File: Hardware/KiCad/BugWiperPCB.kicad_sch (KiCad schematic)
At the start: 11 parts, among them J2 TBLH10-350-06BK, J3 Phoenix_1776508

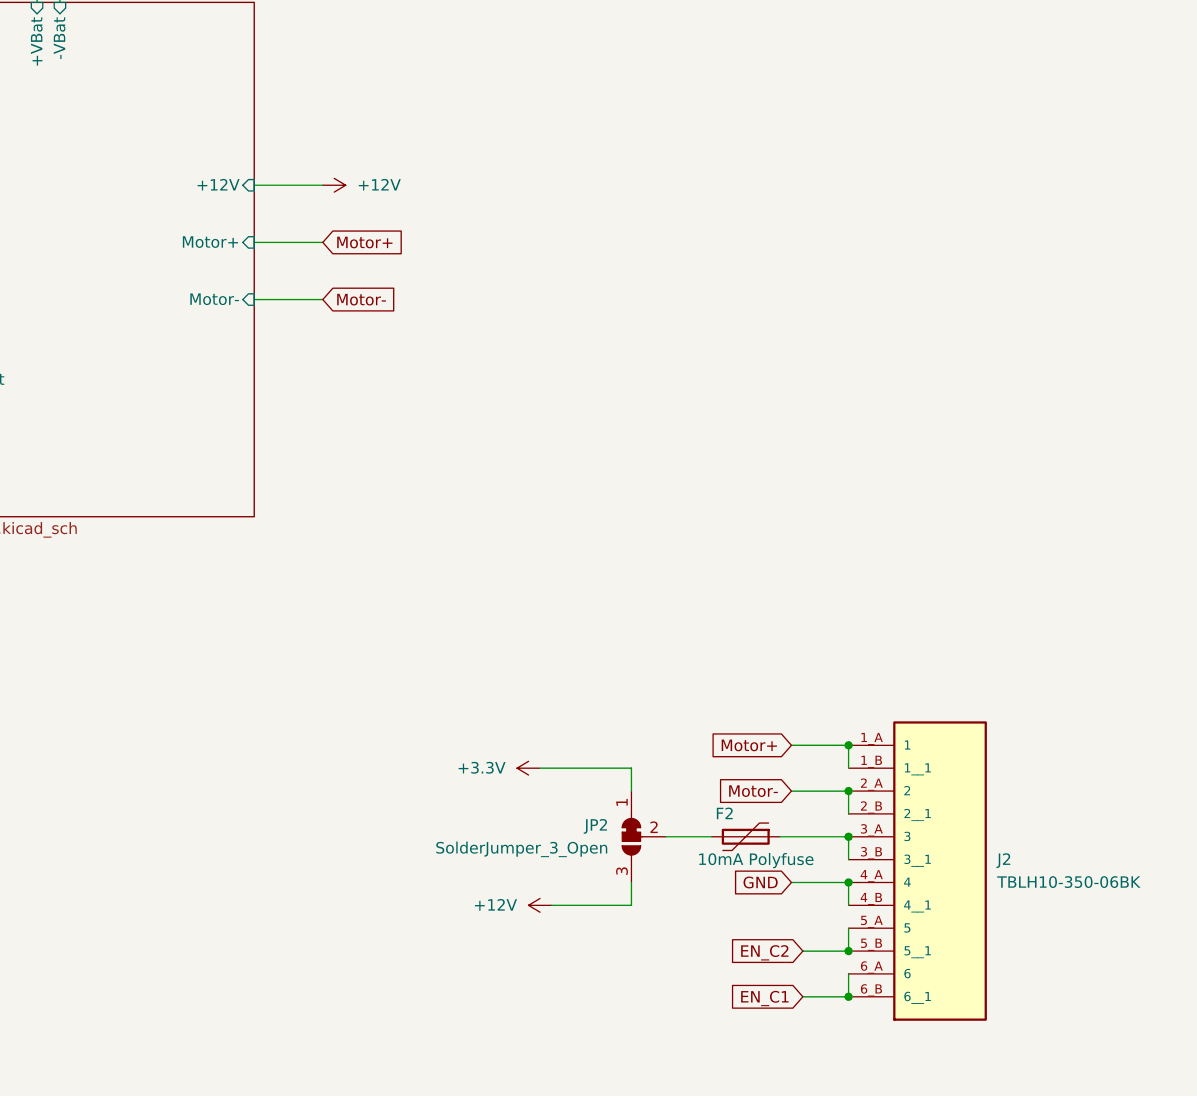
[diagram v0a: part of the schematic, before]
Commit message: update PCB, routing and Connector
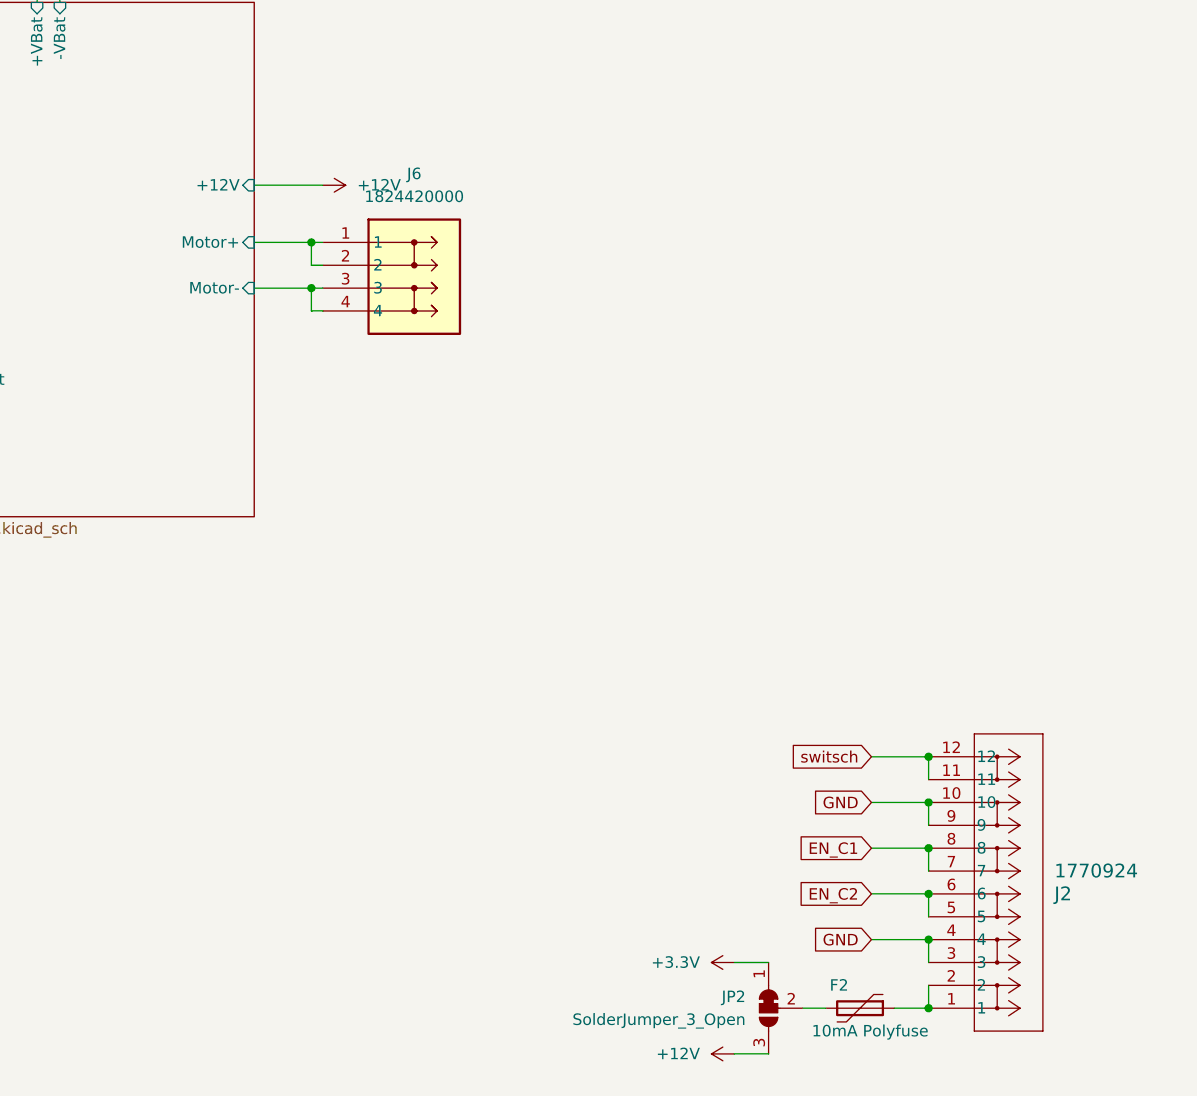
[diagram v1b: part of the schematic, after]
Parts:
- removed J2: TBLH10-350-06BK, TBLH10_350_06BK-2:CUI_TBLH10-350-06BK, symbol TBLH10-350-06BK:TBLH10-350-06BK
- added J2: 1770924, CONN_1814537, symbol BugWiper_Lib:1770924
- added J6: 1824420000, SHDR4W80P700X350_2X2_770X1400X850P, symbol BugWiper_Lib:1824420000
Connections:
- net EN_C1: now also J2.7, J2.8
- net EN_C2: now also J2.5, J2.6
- net GND: now also J2.10, J2.3, J2.4, J2.9
- net at F2.1: now also J2.1, J2.2
- new net Power/Motor+: J6.1, J6.2
- new net Power/Motor-: J6.3, J6.4
- new net switsch: J2.11, J2.12
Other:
- moved on the sheet: F2, JP2

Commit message: update PCB
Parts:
- renumbered H5 to H2, H2 to H5
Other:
- moved on the sheet: C27, H2, H5, R27
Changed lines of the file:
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@@
 (kicad_sch (version 20230121) (generator eeschema)
   (paper "A4")
-  (junction (at 81.28 158.75) (diameter 0) (color 0 0 0 0)
-  )
-  (junction (at 81.28 148.59) (diameter 0) (color 0 0 0 0)
+  (junction (at 114.3 176.53) (diameter 0) (color 0 0 0 0)
+  )
+  (junction (at 114.3 166.37) (diameter 0) (color 0 0 0 0)
   )
   (junction (at 255.27 151.13) (diameter 0) (color 0 0 0 0)
@@
     (stroke (width 0) (type default))
   )
-  (wire (pts (xy 77.47 158.75) (xy 77.47 157.48))
+  (wire (pts (xy 110.49 176.53) (xy 110.49 175.26))
     (stroke (width 0) (type default))
   )
@@
     (stroke (width 0) (type default))
   )
-  (wire (pts (xy 81.28 158.75) (xy 81.28 160.02))
+  (wire (pts (xy 114.3 176.53) (xy 114.3 177.8))
     (stroke (width 0) (type default))
   )
@@
     (stroke (width 0) (type default))
   )
-  (wire (pts (xy 77.47 148.59) (xy 81.28 148.59))
+  (wire (pts (xy 110.49 166.37) (xy 114.3 166.37))
     (stroke (width 0) (type default))
   )
@@
     (stroke (width 0) (type default))
   )
-  (wire (pts (xy 81.28 158.75) (xy 81.28 157.48))
-    (stroke (width 0) (type default))
-  )
-  (wire (pts (xy 77.47 158.75) (xy 81.28 158.75))
+  (wire (pts (xy 114.3 176.53) (xy 114.3 175.26))
+    (stroke (width 0) (type default))
+  )
+  (wire (pts (xy 110.49 176.53) (xy 114.3 176.53))
     (stroke (width 0) (type default))
   )
@@
     (stroke (width 0) (type default))
   )
-  (wire (pts (xy 81.28 148.59) (xy 81.28 149.86))
-    (stroke (width 0) (type default))
-  )
-  (wire (pts (xy 77.47 148.59) (xy 77.47 149.86))
+  (wire (pts (xy 114.3 166.37) (xy 114.3 167.64))
+    (stroke (width 0) (type default))
+  )
+  (wire (pts (xy 110.49 166.37) (xy 110.49 167.64))
     (stroke (width 0) (type default))
   )
@@
     )
   )
-  (symbol (lib_id "Device:C") (at 77.47 153.67 0) (mirror y) (unit 1)
+  (symbol (lib_id "Device:C") (at 110.49 171.45 0) (mirror y) (unit 1)
     (in_bom yes) (on_board yes) (dnp no)
-    (property "Reference" "C27" (at 73.66 152.4 0)
-      (effects (font (size 1.27 1.27)) (justify left))
-    )
-    (property "Value" "100nF" (at 73.66 154.94 0)
-      (effects (font (size 1.27 1.27)) (justify left))
-    )
-    (property "Footprint" "Capacitor_SMD:C_0603_1608Metric" (at 76.5048 157.48 0)
-      (effects (font (size 1.27 1.27)) hide)
-    )
-    (property "Datasheet" "~" (at 77.47 153.67 0)
+    (property "Reference" "C27" (at 106.68 170.18 0)
+      (effects (font (size 1.27 1.27)) (justify left))
+    )
+    (property "Value" "100nF" (at 106.68 172.72 0)
+      (effects (font (size 1.27 1.27)) (justify left))
+    )
+    (property "Footprint" "Capacitor_SMD:C_0603_1608Metric" (at 109.5248 175.26 0)
+      (effects (font (size 1.27 1.27)) hide)
+    )
+    (property "Datasheet" "~" (at 110.49 171.45 0)
       (effects (font (size 1.27 1.27)) hide)
     )
@@
     )
   )
-  (symbol (lib_id "Mechanical:MountingHole_Pad") (at 81.28 146.05 0) (unit 1)
-    (in_bom yes) (on_board yes) (dnp no) (fields_autoplaced)
-    (property "Reference" "H2" (at 83.82 143.51 0)
-      (effects (font (size 1.27 1.27)) (justify left))
-    )
-    (property "Value" "MountingHole_Pad" (at 83.82 146.05 0)
-      (effects (font (size 1.27 1.27)) (justify left))
-    )
-    (property "Footprint" "MountingHole:MountingHole_3.2mm_M3_DIN965_Pad_TopBottom" (at 81.28 146.05 0)
-      (effects (font (size 1.27 1.27)) hide)
-    )
-    (property "Datasheet" "~" (at 81.28 146.05 0)
-      (effects (font (size 1.27 1.27)) hide)
-    )
-    (pin "1")
+  (symbol (lib_id "Mechanical:MountingHole_Pad") (at 114.3 163.83 0) (unit 1)
+    (in_bom yes) (on_board yes) (dnp no) (fields_autoplaced)
+    (property "Reference" "H5" (at 116.84 161.29 0)
+      (effects (font (size 1.27 1.27)) (justify left))
+    )
+    (property "Value" "MountingHole_Pad" (at 116.84 163.83 0)
+      (effects (font (size 1.27 1.27)) (justify left))
+    )
+    (property "Footprint" "MountingHole:MountingHole_3.2mm_M3_DIN965_Pad_TopBottom" (at 114.3 163.83 0)
+      (effects (font (size 1.27 1.27)) hide)
+    )
+    (property "Datasheet" "~" (at 114.3 163.83 0)
+      (effects (font (size 1.27 1.27)) hide)
+    )
+    (pin "1")
+    (instances
+      (project "BugWiperPCB"
+        (path "/d31a15bd-db02-4d4c-9593-17c596d3182c"
+          (reference "H5") (unit 1)
+        )
+      )
+    )
+  )
+  (symbol (lib_id "power:GND") (at 114.3 177.8 0) (unit 1)
+    (in_bom yes) (on_board yes) (dnp no) (fields_autoplaced)
+    (property "Reference" "#PWR034" (at 114.3 184.15 0)
+      (effects (font (size 1.27 1.27)) hide)
+    )
+    (property "Value" "GND" (at 114.3 182.88 0)
+      (effects (font (size 1.27 1.27)))
+    )
+    (property "Footprint" "" (at 114.3 177.8 0)
+      (effects (font (size 1.27 1.27)) hide)
+    )
+    (property "Datasheet" "" (at 114.3 177.8 0)
+      (effects (font (size 1.27 1.27)) hide)
+    )
+    (pin "1")
+    (instances
+      (project "BugWiperPCB"
+        (path "/d31a15bd-db02-4d4c-9593-17c596d3182c"
+          (reference "#PWR034") (unit 1)
+        )
+      )
+    )
+  )
+  (symbol (lib_id "Mechanical:MountingHole") (at 82.55 144.78 0) (unit 1)
+    (in_bom yes) (on_board yes) (dnp no) (fields_autoplaced)
+    (property "Reference" "H2" (at 85.09 143.51 0)
+      (effects (font (size 1.27 1.27)) (justify left))
+    )
+    (property "Value" "MountingHole" (at 85.09 146.05 0)
+      (effects (font (size 1.27 1.27)) (justify left))
+    )
+    (property "Footprint" "MountingHole:MountingHole_3.2mm_M3_DIN965" (at 82.55 144.78 0)
+      (effects (font (size 1.27 1.27)) hide)
+    )
+    (property "Datasheet" "~" (at 82.55 144.78 0)
+      (effects (font (size 1.27 1.27)) hide)
+    )
     (instances
       (project "BugWiperPCB"
@@
     )
   )
-  (symbol (lib_id "power:GND") (at 81.28 160.02 0) (unit 1)
-    (in_bom yes) (on_board yes) (dnp no) (fields_autoplaced)
-    (property "Reference" "#PWR034" (at 81.28 166.37 0)
-      (effects (font (size 1.27 1.27)) hide)
-    )
-    (property "Value" "GND" (at 81.28 165.1 0)
-      (effects (font (size 1.27 1.27)))
-    )
-    (property "Footprint" "" (at 81.28 160.02 0)
-      (effects (font (size 1.27 1.27)) hide)
-    )
-    (property "Datasheet" "" (at 81.28 160.02 0)
-      (effects (font (size 1.27 1.27)) hide)
-    )
-    (pin "1")
-    (instances
-      (project "BugWiperPCB"
-        (path "/d31a15bd-db02-4d4c-9593-17c596d3182c"
-          (reference "#PWR034") (unit 1)
-        )
-      )
-    )
-  )
-  (symbol (lib_id "Mechanical:MountingHole") (at 114.3 162.56 0) (unit 1)
-    (in_bom yes) (on_board yes) (dnp no) (fields_autoplaced)
-    (property "Reference" "H5" (at 116.84 161.29 0)
-      (effects (font (size 1.27 1.27)) (justify left))
-    )
-    (property "Value" "MountingHole" (at 116.84 163.83 0)
-      (effects (font (size 1.27 1.27)) (justify left))
-    )
-    (property "Footprint" "MountingHole:MountingHole_3.2mm_M3_DIN965" (at 114.3 162.56 0)
-      (effects (font (size 1.27 1.27)) hide)
-    )
-    (property "Datasheet" "~" (at 114.3 162.56 0)
-      (effects (font (size 1.27 1.27)) hide)
-    )
-    (instances
-      (project "BugWiperPCB"
-        (path "/d31a15bd-db02-4d4c-9593-17c596d3182c"
-          (reference "H5") (unit 1)
-        )
-      )
-    )
-  )
-  (symbol (lib_id "Device:R") (at 81.28 153.67 0) (unit 1)
-    (in_bom yes) (on_board yes) (dnp no) (fields_autoplaced)
-    (property "Reference" "R27" (at 83.82 152.4 0)
-      (effects (font (size 1.27 1.27)) (justify left))
-    )
-    (property "Value" "1k" (at 83.82 154.94 0)
-      (effects (font (size 1.27 1.27)) (justify left))
-    )
-    (property "Footprint" "Resistor_SMD:R_0603_1608Metric" (at 79.502 153.67 90)
-      (effects (font (size 1.27 1.27)) hide)
-    )
-    (property "Datasheet" "~" (at 81.28 153.67 0)
-      (effects (font (size 1.27 1.27)) hide)
-    )
+  (symbol (lib_id "Device:R") (at 114.3 171.45 0) (unit 1)
+    (in_bom yes) (on_board yes) (dnp no) (fields_autoplaced)
+    (property "Reference" "R27" (at 116.84 170.18 0)
+      (effects (font (size 1.27 1.27)) (justify left))
+    )
+    (property "Value" "1k" (at 116.84 172.72 0)
+      (effects (font (size 1.27 1.27)) (justify left))
+    )
+    (property "Footprint" "Resistor_SMD:R_0603_1608Metric" (at 112.522 171.45 90)
+      (effects (font (size 1.27 1.27)) hide)
+    )
+    (property "Datasheet" "~" (at 114.3 171.45 0)
+      (effects (font (size 1.27 1.27)) hide)
+    )

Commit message: routing
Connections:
- net switsch renamed sw_1
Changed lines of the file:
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@@
     )
   )
-  (global_label "switsch" (shape input) (at 248.92 130.81 180) (fields_autoplaced)
+  (global_label "sw_1" (shape input) (at 248.92 130.81 180) (fields_autoplaced)
     (effects (font (size 1.27 1.27)) (justify right))
-    (property "Intersheetrefs" "${INTERSHEET_REFS}" (at 238.98 130.81 0)
+    (property "Intersheetrefs" "${INTERSHEET_REFS}" (at 241.3991 130.81 0)
       (effects (font (size 1.27 1.27)) (justify right) hide)
     )

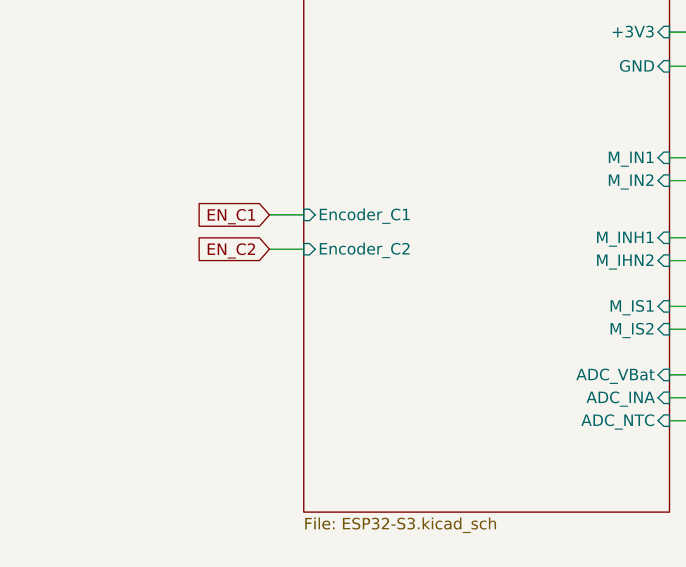
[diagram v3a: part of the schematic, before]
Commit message: routing and change to 4 layer PCB
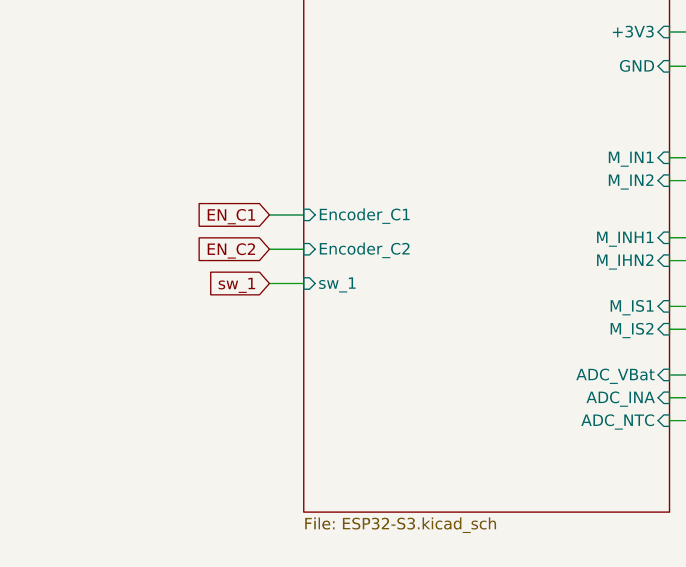
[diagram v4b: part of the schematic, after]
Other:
- sheet ESP32-S3 ports: added sw_1; removed none
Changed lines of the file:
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@@
+    (stroke (width 0) (type default))
+  )
+  (wire (pts (xy 72.39 78.74) (xy 76.2 78.74))
     (stroke (width 0) (type default))
   )
@@
     (effects (font (size 1.27 1.27)) (justify right))
     (property "Intersheetrefs" "${INTERSHEET_REFS}" (at 242.0643 135.89 0)
+      (effects (font (size 1.27 1.27)) (justify right) hide)
+    )
+  )
+  (global_label "sw_1" (shape input) (at 72.39 78.74 180) (fields_autoplaced)
+    (effects (font (size 1.27 1.27)) (justify right))
+    (property "Intersheetrefs" "${INTERSHEET_REFS}" (at 64.8691 78.74 0)
       (effects (font (size 1.27 1.27)) (justify right) hide)
     )
@@
       (effects (font (size 1.27 1.27)) (justify right))
     )
-    (instances
+    (pin "sw_1" input (at 76.2 78.74 180)
+      (effects (font (size 1.27 1.27)) (justify left))
+    )
+    (instances
